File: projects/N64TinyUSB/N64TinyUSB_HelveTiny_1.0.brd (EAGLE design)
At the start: 20.1 x 37.3 mm, 24 parts, among them U1 ATTINY85-20PU

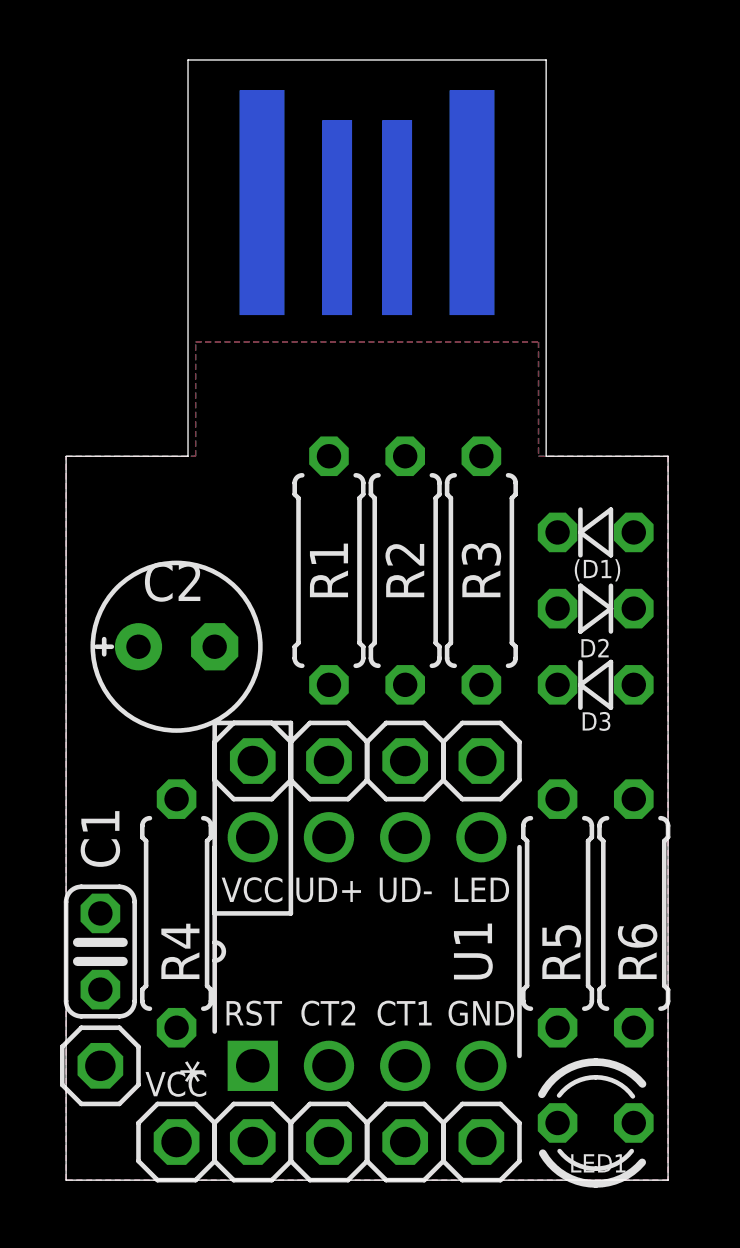
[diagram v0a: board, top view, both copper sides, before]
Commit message: clean-up; * finish travis config           * use routed version of pcb
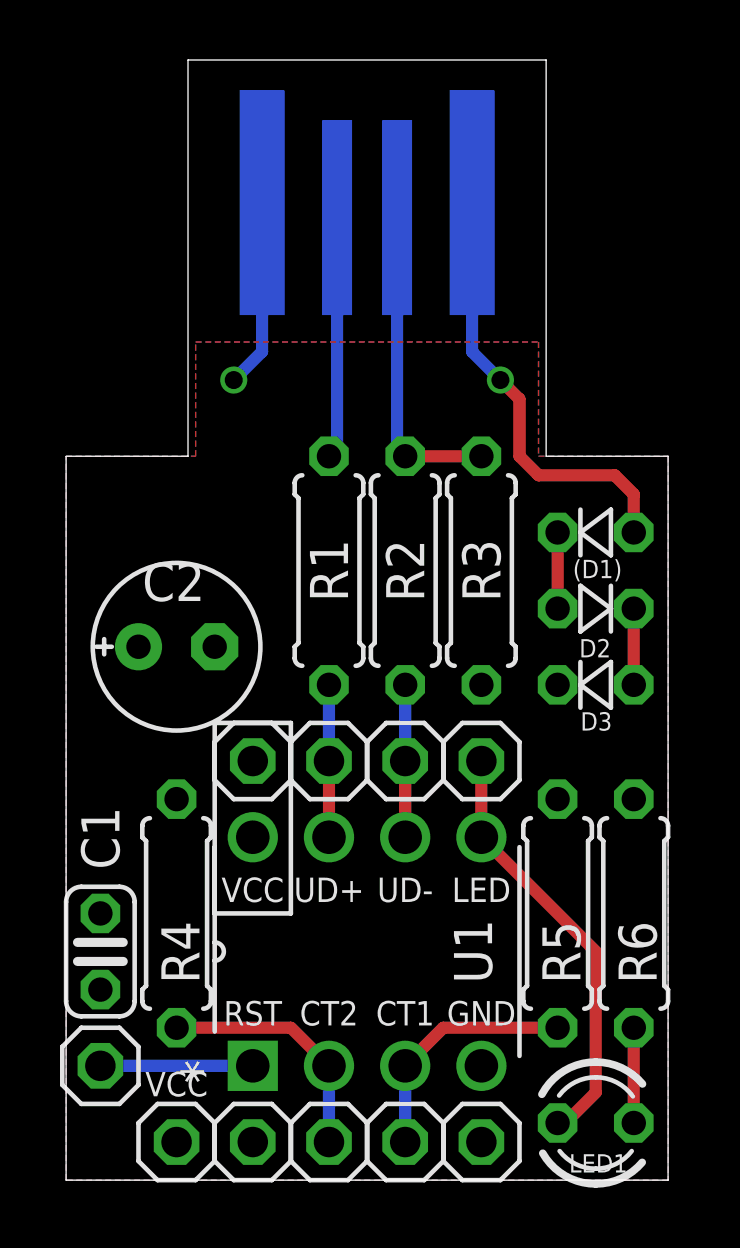
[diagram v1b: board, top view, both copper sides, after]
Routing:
- net N$9: track 0.00 -> 14.7 mm, vias 0 -> 1
- net N$6: track 0.00 -> 14.3 mm
- net N$3: track 0.00 -> 10.6 mm
- net CTRL2: track 0.00 -> 8.15 mm
- net CTRL1: track 0.00 -> 8.15 mm
- net N$4: track 0.00 -> 8.07 mm
- net GND: track 0.00 -> 6.31 mm, vias 0 -> 1
- net RST: track 0.00 -> 5.08 mm
- net N$8: track 0.00 -> 5.08 mm
- net N$7: track 0.00 -> 5.08 mm
- net N$15: track 0.00 -> 3.17 mm
- net N$11: track 0.00 -> 2.54 mm
- net N$10: track 0.00 -> 2.54 mm
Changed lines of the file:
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@@
 <contactref element="VCC1" pad="1"/>
 <contactref element="VCC2" pad="1"/>
-<wire x1="13.335" y1="15.24" x2="15.875" y2="15.24" width="0" layer="19" extent="1-1"/>
-<wire x1="15.875" y1="11.43" x2="15.875" y2="15.24" width="0" layer="19" extent="1-1"/>
-<wire x1="5.715" y1="12.7" x2="13.335" y2="15.24" width="0" layer="19" extent="1-1"/>
-<wire x1="5.715" y1="10.16" x2="5.715" y2="12.7" width="0" layer="19" extent="1-1"/>
-<wire x1="3.175" y1="11.43" x2="5.715" y2="12.7" width="0" layer="19" extent="1-1"/>
-<wire x1="0.635" y1="7.62" x2="3.175" y2="11.43" width="0" layer="19" extent="1-1"/>
-<wire x1="1.905" y1="16.51" x2="3.175" y2="11.43" width="0" layer="19" extent="1-1"/>
-<wire x1="3.175" y1="0" x2="0.635" y2="7.62" width="0" layer="19" extent="1-1"/>
 </signal>
 <signal name="CTRL2">
 <contactref element="U1" pad="2"/>
 <contactref element="R4" pad="1"/>
+<wire x1="3.175" y1="3.81" x2="6.985" y2="3.81" width="0.4064" layer="1"/>
+<wire x1="6.985" y1="3.81" x2="8.255" y2="2.54" width="0.4064" layer="1"/>
 <contactref element="CTRL2" pad="1"/>
-<wire x1="8.255" y1="0" x2="8.255" y2="2.54" width="0" layer="19" extent="1-1"/>
-<wire x1="3.175" y1="3.81" x2="8.255" y2="2.54" width="0" layer="19" extent="1-1"/>
+<wire x1="8.255" y1="0" x2="8.255" y2="2.54" width="0.4064" layer="16"/>
 </signal>
 <signal name="CTRL1">
 <contactref element="U1" pad="3"/>
 <contactref element="R5" pad="1"/>
+<wire x1="15.875" y1="3.81" x2="12.065" y2="3.81" width="0.4064" layer="1"/>
+<wire x1="12.065" y1="3.81" x2="10.795" y2="2.54" width="0.4064" layer="1"/>
 <contactref element="CTRL1" pad="1"/>
-<wire x1="10.795" y1="2.54" x2="15.875" y2="3.81" width="0" layer="19" extent="1-1"/>
-<wire x1="10.795" y1="0" x2="10.795" y2="2.54" width="0" layer="19" extent="1-1"/>
+<wire x1="10.795" y1="0" x2="10.795" y2="2.54" width="0.4064" layer="16"/>
 </signal>
 <signal name="N$3">
@@
 <contactref element="JP1" pad="USB_M"/>
 <contactref element="R3" pad="1"/>
-<wire x1="10.795" y1="22.86" x2="10.525" y2="30.815" width="0" layer="19" extent="16-16"/>
-<wire x1="13.335" y1="22.86" x2="10.795" y2="22.86" width="0" layer="19" extent="1-1"/>
+<wire x1="13.335" y1="22.86" x2="10.795" y2="22.86" width="0.4064" layer="1"/>
+<wire x1="10.525" y1="30.815" x2="10.525" y2="23.13" width="0.4064" layer="16"/>
+<wire x1="10.525" y1="23.13" x2="10.795" y2="22.86" width="0.4064" layer="16"/>
 </signal>
 <signal name="N$4">
 <contactref element="R1" pad="1"/>
 <contactref element="JP1" pad="USB_P"/>
-<wire x1="8.255" y1="22.86" x2="8.525" y2="30.815" width="0" layer="19" extent="16-16"/>
+<wire x1="8.525" y1="30.815" x2="8.525" y2="23.13" width="0.4064" layer="16"/>
+<wire x1="8.525" y1="23.13" x2="8.255" y2="22.86" width="0.4064" layer="16"/>
 </signal>
 <signal name="GND">
@@
 <contactref element="C2" pad="-"/>
 <contactref element="R6" pad="1"/>
+<via x="5.08" y="25.4" extent="1-16" drill="0.6"/>
 <contactref element="GND" pad="1"/>
-<wire x1="4.445" y1="16.51" x2="6.025" y2="31.315" width="0" layer="19" extent="16-16"/>
-<wire x1="0.635" y1="5.08" x2="4.445" y2="16.51" width="0" layer="19" extent="1-1"/>
-<wire x1="13.335" y1="2.54" x2="0.635" y2="5.08" width="0" layer="19" extent="1-1"/>
-<wire x1="13.335" y1="0" x2="13.335" y2="2.54" width="0" layer="19" extent="1-1"/>
-<wire x1="18.415" y1="11.43" x2="13.335" y2="2.54" width="0" layer="19" extent="1-1"/>
+<wire x1="6.025" y1="31.315" x2="6.025" y2="26.345" width="0.4064" layer="16"/>
+<wire x1="6.025" y1="26.345" x2="5.08" y2="25.4" width="0.4064" layer="16"/>
 </signal>
 <signal name="RST">
 <contactref element="U1" pad="1"/>
 <contactref element="RST" pad="1"/>
-<wire x1="0.635" y1="2.54" x2="5.715" y2="2.54" width="0" layer="19" extent="1-1"/>
+<wire x1="0.635" y1="2.54" x2="5.715" y2="2.54" width="0.4064" layer="16"/>
 </signal>
 <signal name="N$6">
 <contactref element="U1" pad="5"/>
 <contactref element="LED1" pad="A"/>
+<wire x1="15.875" y1="0.635" x2="16.129" y2="0.635" width="0.4064" layer="1"/>
+<wire x1="16.129" y1="0.635" x2="17.145" y2="1.651" width="0.4064" layer="1"/>
+<wire x1="17.145" y1="1.651" x2="17.145" y2="6.35" width="0.4064" layer="1"/>
+<wire x1="17.145" y1="6.35" x2="13.335" y2="10.16" width="0.4064" layer="1"/>
 <contactref element="LED" pad="1"/>
-<wire x1="13.335" y1="10.16" x2="13.335" y2="12.7" width="0" layer="19" extent="1-1"/>
-<wire x1="15.875" y1="0.635" x2="13.335" y2="10.16" width="0" layer="19" extent="1-1"/>
+<wire x1="13.335" y1="12.7" x2="13.335" y2="10.16" width="0.4064" layer="1"/>
 </signal>
 <signal name="N$7">
@@
 <contactref element="U1" pad="6"/>
 <contactref element="D-" pad="1"/>
-<wire x1="10.795" y1="12.7" x2="10.795" y2="15.24" width="0" layer="19" extent="1-1"/>
-<wire x1="10.795" y1="10.16" x2="10.795" y2="12.7" width="0" layer="19" extent="1-1"/>
+<wire x1="10.795" y1="15.24" x2="10.795" y2="12.7" width="0.4064" layer="16"/>
+<wire x1="10.795" y1="12.7" x2="10.795" y2="10.16" width="0.4064" layer="1"/>
 </signal>
 <signal name="N$8">
@@
 <contactref element="R1" pad="2"/>
 <contactref element="D+" pad="1"/>
-<wire x1="8.255" y1="12.7" x2="8.255" y2="15.24" width="0" layer="19" extent="1-1"/>
-<wire x1="8.255" y1="10.16" x2="8.255" y2="12.7" width="0" layer="19" extent="1-1"/>
+<wire x1="8.255" y1="15.24" x2="8.255" y2="12.7" width="0.4064" layer="16"/>
+<wire x1="8.255" y1="12.7" x2="8.255" y2="10.16" width="0.4064" layer="1"/>
 </signal>
 <signal name="N$9">
 <contactref element="JP1" pad="5V"/>
 <contactref element="(D1)" pad="A"/>
-<wire x1="18.415" y1="20.32" x2="13.025" y2="31.315" width="0" layer="19" extent="16-16"/>
+<via x="13.97" y="25.4" extent="1-16" drill="0.6"/>
+<wire x1="13.025" y1="31.315" x2="13.025" y2="26.345" width="0.4064" layer="16"/>
+<wire x1="13.025" y1="26.345" x2="13.97" y2="25.4" width="0.4064" layer="16"/>
+<wire x1="13.97" y1="25.4" x2="14.605" y2="24.765" width="0.4064" layer="1"/>
+<wire x1="14.605" y1="24.765" x2="14.605" y2="22.86" width="0.4064" layer="1"/>
+<wire x1="14.605" y1="22.86" x2="15.24" y2="22.225" width="0.4064" layer="1"/>
+<wire x1="15.24" y1="22.225" x2="17.78" y2="22.225" width="0.4064" layer="1"/>
+<wire x1="17.78" y1="22.225" x2="18.415" y2="21.59" width="0.4064" layer="1"/>
+<wire x1="18.415" y1="21.59" x2="18.415" y2="20.32" width="0.4064" layer="1"/>
 </signal>
 <signal name="N$15">
 <contactref element="LED1" pad="K"/>
 <contactref element="R6" pad="2"/>
-<wire x1="18.415" y1="0.635" x2="18.415" y2="3.81" width="0" layer="19" extent="1-1"/>
+<wire x1="18.415" y1="3.81" x2="18.415" y2="0.635" width="0.4064" layer="1"/>
 </signal>
 <signal name="N$10">
 <contactref element="(D1)" pad="C"/>
 <contactref element="D2" pad="A"/>
-<wire x1="15.875" y1="17.78" x2="15.875" y2="20.32" width="0" layer="19" extent="1-1"/>
+<wire x1="15.875" y1="20.32" x2="15.875" y2="17.78" width="0.4064" layer="1"/>
 </signal>
 <signal name="N$11">
 <contactref element="D2" pad="C"/>
 <contactref element="D3" pad="A"/>
-<wire x1="18.415" y1="15.24" x2="18.415" y2="17.78" width="0" layer="19" extent="1-1"/>
+<wire x1="18.415" y1="17.78" x2="18.415" y2="15.24" width="0.4064" layer="1"/>
 </signal>
 </signals>
